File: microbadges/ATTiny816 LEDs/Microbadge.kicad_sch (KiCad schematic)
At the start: 13 parts, among them U1 ATtiny816-M

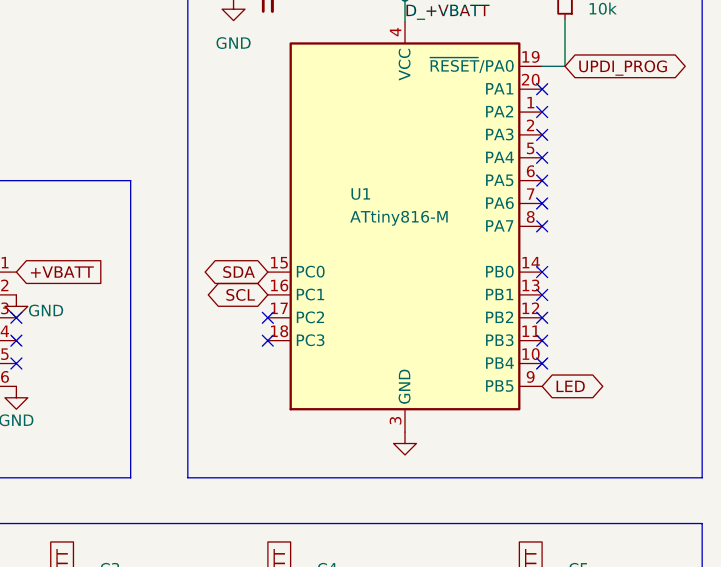
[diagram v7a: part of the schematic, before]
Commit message: Update I2C pins
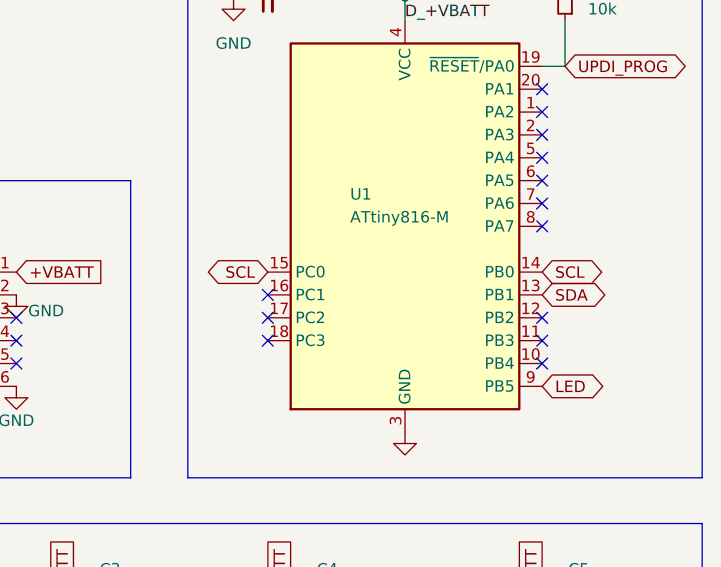
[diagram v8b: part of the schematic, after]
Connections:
- net SCL: now also U1.14 (PB0), U1.15 (PC0); no longer U1.16 (PC1)
- net SDA: now also U1.13 (PB1); no longer U1.15 (PC0)
- no-connect marks 19 -> 18
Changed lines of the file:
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@@
+	)
+	(no_connect
+		(at 152.4 82.55)
 	)
 	(no_connect
@@
 	)
 	(no_connect
-		(at 182.88 77.47)
+		(at 182.88 85.09)
+	)
+	(no_connect
+		(at 182.88 67.31)
+	)
+	(no_connect
+		(at 182.88 72.39)
+	)
+	(no_connect
+		(at 101.6 87.63)
+	)
+	(no_connect
+		(at 182.88 62.23)
+	)
+	(no_connect
+		(at 152.4 80.01)
 	)
 	(no_connect
 		(at 152.4 85.09)
-	)
-	(no_connect
-		(at 182.88 85.09)
-	)
-	(no_connect
-		(at 182.88 67.31)
-	)
-	(no_connect
-		(at 182.88 72.39)
-	)
-	(no_connect
-		(at 101.6 87.63)
-	)
-	(no_connect
-		(at 182.88 62.23)
-	)
-	(no_connect
-		(at 182.88 80.01)
-	)
-	(no_connect
-		(at 152.4 82.55)
 	)
 	(no_connect
@@
 		)
 	)
+	(global_label "SCL"
+		(shape bidirectional)
+		(at 152.4 77.47 180)
+		(fields_autoplaced yes)
+		(effects
+			(font
+				(size 1.27 1.27)
+			)
+			(justify right)
+		)
+		(property "Intersheetrefs" "${INTERSHEET_REFS}"
+			(at 144.7959 77.47 0)
+			(effects
+				(font
+					(size 1.27 1.27)
+				)
+				(justify right)
+				(hide yes)
+			)
+		)
+	)
 	(global_label "CLK"
 		(shape bidirectional)
@@
 	(global_label "SDA"
 		(shape bidirectional)
-		(at 152.4 77.47 180)
-		(fields_autoplaced yes)
-		(effects
-			(font
-				(size 1.27 1.27)
-			)
-			(justify right)
-		)
-		(property "Intersheetrefs" "${INTERSHEET_REFS}"
-			(at 144.7354 77.47 0)
-			(effects
-				(font
-					(size 1.27 1.27)
-				)
-				(justify right)
+		(at 182.88 80.01 0)
+		(fields_autoplaced yes)
+		(effects
+			(font
+				(size 1.27 1.27)
+			)
+			(justify left)
+		)
+		(property "Intersheetrefs" "${INTERSHEET_REFS}"
+			(at 190.4841 80.01 0)
+			(effects
+				(font
+					(size 1.27 1.27)
+				)
+				(justify left)
+				(hide yes)
+			)
+		)
+	)
+	(global_label "SCL"
+		(shape bidirectional)
+		(at 182.88 77.47 0)
+		(fields_autoplaced yes)
+		(effects
+			(font
+				(size 1.27 1.27)
+			)
+			(justify left)
+		)
+		(property "Intersheetrefs" "${INTERSHEET_REFS}"
+			(at 190.5446 77.47 0)
+			(effects
+				(font
+					(size 1.27 1.27)
+				)
+				(justify left)
 				(hide yes)
 			)
@@
 			(effects
 				(font
-					(size 1.27 1.27)
-				)
-				(justify right)
-				(hide yes)
-			)
-		)
-	)
-	(global_label "SCL"
-		(shape bidirectional)
-		(at 152.4 80.01 180)
-		(fields_autoplaced yes)
-		(effects
-			(font
-				(size 1.27 1.27)
-			)
-			(justify right)
-		)
-		(property "Intersheetrefs" "${INTERSHEET_REFS}"
-			(at 144.7959 80.01 0)
-			(effects
-				(font
